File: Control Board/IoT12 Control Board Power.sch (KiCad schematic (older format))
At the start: 17 parts, among them U5 LM2596S-ADJ

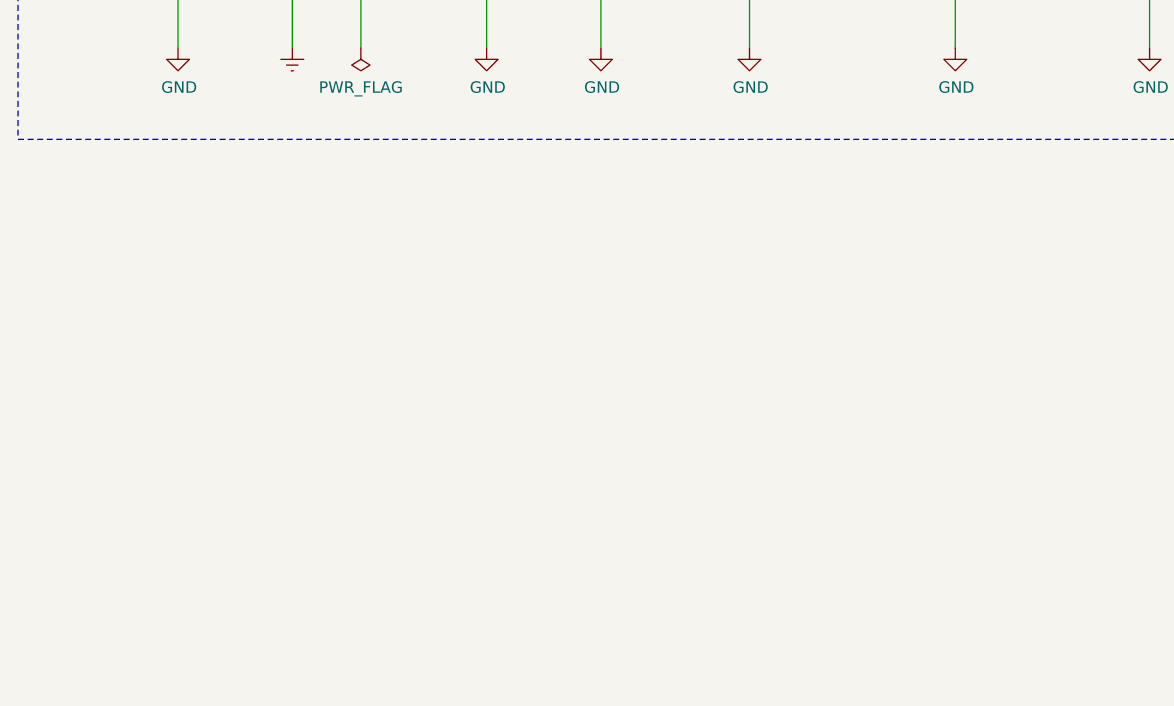
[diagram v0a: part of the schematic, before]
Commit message: More testing and re-added voltage monitor.
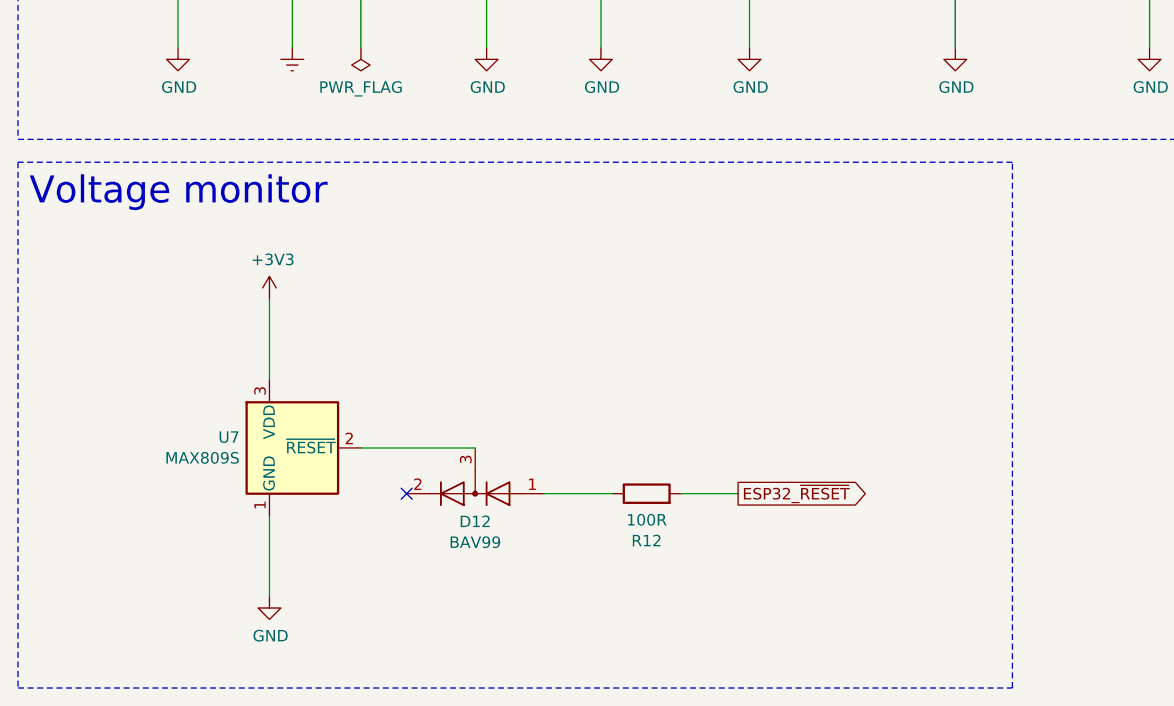
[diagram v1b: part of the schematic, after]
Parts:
- added D12: BAV99, Package_TO_SOT_SMD:SOT-23, symbol Diode:BAV99
- added R12: 100R, Resistor_SMD:R_0805_2012Metric_Pad1.20x1.40mm_HandSolder, symbol Device:R
- added U7: MAX809S, Package_TO_SOT_SMD:SOT-23, symbol Power_Supervisor:TPS3839DBZ
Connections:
- net GND: now also U7.1 (GND)
- new net: D12.3 (K), U7.2 (~RESET)
- new net: D12.1 (K), R12.1
- new net +3V3: U7.3 (VDD)
- new net ESP32_~RESET: R12.2
- no-connect marks 0 -> 1
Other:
- note added: "Voltage monitor"
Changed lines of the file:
@@
 Wire Wire Line
 	1250 1950 1250 3300
+$Comp
+L Power_Supervisor:TPS3839DBZ U7
+U 1 1 604FCB6B
+P 1650 5050
+F 0 "U7" H 1520 5096 50  0000 R CNN
+F 1 "MAX809S" H 1520 5005 50  0000 R CNN
+F 2 "Package_TO_SOT_SMD:SOT-23" H 1650 5050 50  0001 C CNN
+F 3 "" H 1650 5050 50  0001 C CNN
+	1    1650 5050
+	1    0    0    -1
+$EndComp
+$Comp
+L Diode:BAV99 D12
+U 1 1 604FD0FA
+P 2550 5250
+F 0 "D12" H 2550 5373 50  0000 C CNN
+F 1 "BAV99" H 2550 5464 50  0000 C CNN
+F 2 "Package_TO_SOT_SMD:SOT-23" H 2550 4750 50  0001 C CNN
+F 3 "https://assets.nexperia.com/documents/data-sheet/BAV99_SER.pdf" H 2550 5250 50  0001 C CNN
+	1    2550 5250
+	-1   0    0    1
+$EndComp
+$Comp
+L power:GND #PWR0136
+U 1 1 60501446
+P 1650 5700
+F 0 "#PWR0136" H 1650 5450 50  0001 C CNN
+F 1 "GND" H 1655 5527 50  0000 C CNN
+F 2 "" H 1650 5700 50  0001 C CNN
+F 3 "" H 1650 5700 50  0001 C CNN
+	1    1650 5700
+	1    0    0    -1
+$EndComp
+$Comp
+L power:+3V3 #PWR0179
+U 1 1 60501A96
+P 1650 4400
+F 0 "#PWR0179" H 1650 4250 50  0001 C CNN
+F 1 "+3V3" H 1665 4573 50  0000 C CNN
+F 2 "" H 1650 4400 50  0001 C CNN
+F 3 "" H 1650 4400 50  0001 C CNN
+	1    1650 4400
+	1    0    0    -1
+$EndComp
+Wire Wire Line
+	1650 4750 1650 4400
+Wire Wire Line
+	2550 5050 2050 5050
+Wire Wire Line
+	1650 5350 1650 5700
+NoConn ~ 2250 5250
+$Comp
+L Device:R R12
+U 1 1 60506A5D
+P 3300 5250
+F 0 "R12" V 3093 5250 50  0000 C CNN
+F 1 "100R" V 3184 5250 50  0000 C CNN
+F 2 "Resistor_SMD:R_0805_2012Metric_Pad1.20x1.40mm_HandSolder" V 3230 5250 50  0001 C CNN
+F 3 "~" H 3300 5250 50  0001 C CNN
+	1    3300 5250
+	0    -1   -1   0
+$EndComp
+Wire Wire Line
+	2850 5250 3150 5250
+Text GLabel 3700 5250 2    50   Output ~ 0
+ESP32_~RESET
+Wire Wire Line
+	3450 5250 3700 5250
+Wire Notes Line
+	550  3800 550  6100
+Wire Notes Line
+	550  6100 4900 6100
+Wire Notes Line
+	4900 6100 4900 3800
+Wire Notes Line
+	4900 3800 550  3800
+Text Notes 600  4000 0    118  ~ 0
+Voltage monitor
 $EndSCHEMATC

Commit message: V2.1 changes.
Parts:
- F1: value 2.5A/30V -> *see schematic.
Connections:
- net +24V: now also R70.2
- net at D6.2 (A), F2.1: no longer R70.2
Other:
- note added: "*F1: fuse must be <=50% of amperage of T12 tip.\nFuse Vmax must exceed Vsupply.\nPower supply must be >=100% of amperage of T12 tip.\nMPM-90-24: 1.50A (JK60-150)\nMPM-30-15: 0.90A\nMPM-20-12: 0.75A"
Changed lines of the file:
@@
 Sheet 3 5
 Title "IoT12-hardware power supply"
-Date "2021-03-28"
+Date "2021-04-02"
 Rev "V2.1"
 Comp ""
@@
 Wire Wire Line
 	2600 2300 2600 2500
-Wire Wire Line
-	2600 1750 2650 1750
-Connection ~ 2600 1750
-Wire Wire Line
-	2600 2000 2600 1750
 $Comp
 L power:GND #PWR0124
@@
 P 2100 1550
 F 0 "F1" V 1875 1550 50  0000 C CNN
-F 1 "2.5A/30V" V 1966 1550 50  0000 C CNN
+F 1 "*see schematic." V 1966 1550 50  0000 C CNN
 F 2 "Fuse:Fuse_Bourns_MF-RG1000" H 2150 1350 50  0001 L CNN
 F 3 "~" H 2100 1550 50  0001 C CNN
@@
 $EndComp
 Wire Wire Line
-	2250 1550 2650 1550
+	2250 1550 2600 1550
 Wire Wire Line
 	1750 1750 1950 1750
@@
 Wire Wire Line
 	1150 1750 1750 1750
-Wire Wire Line
-	2250 1750 2600 1750
 Wire Wire Line
 	6650 3300 6650 2650
@@
 	3100 1750 2950 1750
 Wire Wire Line
-	2650 1350 2650 900
-Connection ~ 2650 1350
-Wire Wire Line
-	3000 1350 2650 1350
-Wire Wire Line
-	3000 900  3000 1350
+	3000 1350 3000 900
+Connection ~ 3000 1350
+Wire Wire Line
+	3350 1350 3000 1350
+Wire Wire Line
+	3350 900  3350 1350
 $Comp
 L power:PWR_FLAG #FLG0103
 U 1 1 5FF40C51
-P 3000 900
-F 0 "#FLG0103" H 3000 975 50  0001 C CNN
-F 1 "PWR_FLAG" H 3000 1073 50  0000 C CNN
-F 2 "" H 3000 900 50  0001 C CNN
-F 3 "~" H 3000 900 50  0001 C CNN
-	1    3000 900
-	1    0    0    -1
-$EndComp
-Wire Wire Line
-	2650 1550 2650 1350
+P 3350 900
+F 0 "#FLG0103" H 3350 975 50  0001 C CNN
+F 1 "PWR_FLAG" H 3350 1073 50  0000 C CNN
+F 2 "" H 3350 900 50  0001 C CNN
+F 3 "~" H 3350 900 50  0001 C CNN
+	1    3350 900
+	1    0    0    -1
+$EndComp
+Wire Wire Line
+	3000 1550 3000 1350
 $Comp
 L power:+24V #PWR0120
 U 1 1 5FF3E5BB
-P 2650 900
-F 0 "#PWR0120" H 2650 750 50  0001 C CNN
-F 1 "+24V" H 2665 1073 50  0000 C CNN
-F 2 "" H 2650 900 50  0001 C CNN
-F 3 "" H 2650 900 50  0001 C CNN
-	1    2650 900
+P 3000 900
+F 0 "#PWR0120" H 3000 750 50  0001 C CNN
+F 1 "+24V" H 3015 1073 50  0000 C CNN
+F 2 "" H 3000 900 50  0001 C CNN
+F 3 "" H 3000 900 50  0001 C CNN
+	1    3000 900
 	1    0    0    -1
 $EndComp
@@
 Text Notes 600  4000 0    118  ~ 0
 Voltage monitor
+Text Notes 650  1350 0    50   ~ 0
+*F1: fuse must be <=50% of amperage of T12 tip.\nFuse Vmax must exceed Vsupply.\nPower supply must be >=100% of amperage of T12 tip.\nMPM-90-24: 1.50A (JK60-150)\nMPM-30-15: 0.90A\nMPM-20-12: 0.75A
+Wire Wire Line
+	2250 1750 2650 1750
+Wire Wire Line
+	2600 2000 2600 1550
+Connection ~ 2600 1550
+Wire Wire Line
+	2600 1550 3000 1550
 $EndSCHEMATC

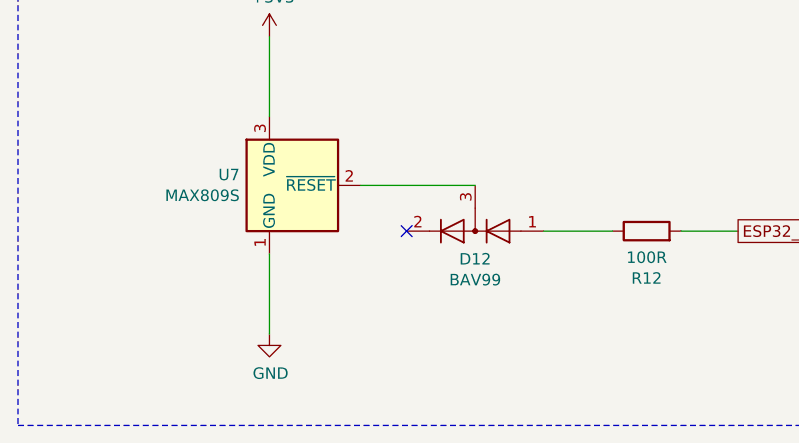
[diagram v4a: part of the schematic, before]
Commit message: Added ~RESET pulldown resistor.
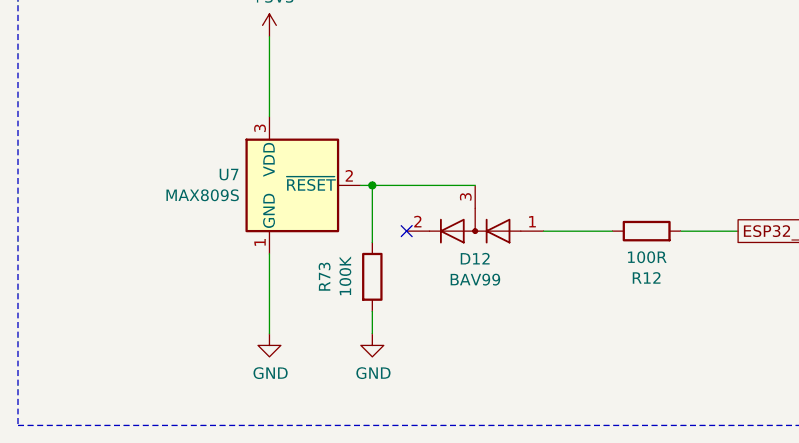
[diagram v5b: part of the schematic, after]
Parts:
- added R73: 100K, Resistor_SMD:R_0805_2012Metric_Pad1.20x1.40mm_HandSolder, symbol Device:R
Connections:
- net GND: now also R73.2
- net at D12.3 (K), U7.2 (~RESET): now also R73.1
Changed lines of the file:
@@
 	1650 4750 1650 4400
 Wire Wire Line
-	2550 5050 2050 5050
+	2550 5050 2100 5050
 Wire Wire Line
 	1650 5350 1650 5700
@@
 Wire Wire Line
 	2600 1550 3000 1550
+$Comp
+L Device:R R73
+U 1 1 6071D566
+P 2100 5450
+F 0 "R73" V 1893 5450 50  0000 C CNN
+F 1 "100K" V 1984 5450 50  0000 C CNN
+F 2 "Resistor_SMD:R_0805_2012Metric_Pad1.20x1.40mm_HandSolder" V 2030 5450 50  0001 C CNN
+F 3 "~" H 2100 5450 50  0001 C CNN
+	1    2100 5450
+	1    0    0    -1
+$EndComp
+$Comp
+L power:GND #PWR0180
+U 1 1 6071E102
+P 2100 5700
+F 0 "#PWR0180" H 2100 5450 50  0001 C CNN
+F 1 "GND" H 2105 5527 50  0000 C CNN
+F 2 "" H 2100 5700 50  0001 C CNN
+F 3 "" H 2100 5700 50  0001 C CNN
+	1    2100 5700
+	1    0    0    -1
+$EndComp
+Wire Wire Line
+	2100 5600 2100 5700
+Wire Wire Line
+	2100 5300 2100 5050
+Connection ~ 2100 5050
+Wire Wire Line
+	2100 5050 2050 5050
 $EndSCHEMATC

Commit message: Changed some footprints to that have 3d models.
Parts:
- L1: footprint Inductor_SMD:L_12x12mm_H8mm -> Inductor-fixed:L_12x12mm_H8mm
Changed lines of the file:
@@
 Sheet 3 5
 Title "IoT12-hardware power supply"
-Date "2021-04-02"
+Date "2021-04-27"
 Rev "V2.1"
 Comp ""
@@
 F 0 "L1" V 5662 1950 50  0000 C CNN
 F 1 "68uH" V 5571 1950 50  0000 C CNN
-F 2 "Inductor_SMD:L_12x12mm_H8mm" H 5750 1950 50  0001 C CNN
+F 2 "Inductor-fixed:L_12x12mm_H8mm" H 5750 1950 50  0001 C CNN
 F 3 "~" H 5750 1950 50  0001 C CNN
 	1    5750 1950
